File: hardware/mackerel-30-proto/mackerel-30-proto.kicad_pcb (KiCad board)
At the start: 2 copper layers, 160 x 100 mm, 73 parts, among them J1 Conn_01x02, J2 Conn_01x02, J3 Conn_02x05_Odd_Even, J4 Barrel_Jack_MountingPin, J5 Conn_02x05_Odd_Even, U1 MC68030RC, U10 MC68882, U2 EPM7128, U3 SST39SF040, U4 AS6C4008-55PCN, U5 XR68C681, U6 LM2576T-5, U7 AMS1117-3.3, U8 EPM7128, U9 SIMM72, X1 CXO_DIP14, X2 3.6864MHz, X3 CXO_DIP14

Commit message: positioning
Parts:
- added C27: C_Polarized, Capacitor_THT:CP_Radial_D5.0mm_P2.50mm, F.Cu at (-78.9, 88.3)
- added C28: C, Capacitor_THT:C_Disc_D4.3mm_W1.9mm_P5.00mm, F.Cu at (-57.9, 91.6)
- added D3: LED, LED_THT:LED_D5.0mm, F.Cu at (-64.5, 93.6)
- added HS1: Heatsink, Heatsink:Heatsink_Stonecold_HS-S02_13.21x9.53mm, F.Cu at (-67.0, 79.6)
- added J10: Conn_02x03_Odd_Even, Connector_PinHeader_2.54mm:PinHeader_2x03_P2.54mm_Vertical, F.Cu at (-64.3, 51.9)
- added J11: Conn_02x05_Odd_Even, Connector_IDC:IDC-Header_2x05_P2.54mm_Vertical, F.Cu at (-122.4, 15.6)
- added J6: Conn_02x10_Odd_Even, Connector_PinHeader_2.54mm:PinHeader_2x10_P2.54mm_Vertical, F.Cu at (-52.7, 103.2)
- added J7: Barrel_Jack_MountingPin, Connector_BarrelJack:BarrelJack_Horizontal, F.Cu at (-66.5, 64.6)
- added J8: Conn_02x03_Odd_Even, Connector_PinHeader_2.54mm:PinHeader_2x03_P2.54mm_Vertical, F.Cu at (-78.7, 51.9)
- added J9: Conn_02x03_Odd_Even, Connector_PinHeader_2.54mm:PinHeader_2x03_P2.54mm_Vertical, F.Cu at (-71.5, 51.9)
- added R23: R, Resistor_SMD:R_0805_2012Metric_Pad1.20x1.40mm_HandSolder, F.Cu at (-113.3, 28.2)
- added R24: R, Resistor_SMD:R_0805_2012Metric_Pad1.20x1.40mm_HandSolder, F.Cu at (-113.3, 31.1)
- added R25: R, Resistor_SMD:R_0805_2012Metric_Pad1.20x1.40mm_HandSolder, F.Cu at (-113.3, 34.1)
- added SW1: SW_Push, Button_Switch_THT:SW_PUSH_6mm_H5mm, F.Cu at (-90.8, 86.4)
- added U11: MC68882, Package_LCC:PLCC-68_THT-Socket, F.Cu at (84.4, 37.4)
- C1, C10, C11, C12, C13, C14, C15, C16, C17, C18, C19, C2, C20, C21, C22, C3, C4, C5, C6, C7, C8, C9: footprint Capacitor_SMD:C_1210_3225Metric_Pad1.33x2.70mm_HandSolder -> Capacitor_SMD:C_1206_3216Metric_Pad1.33x1.80mm_HandSolder
- J4: value Barrel_Jack_MountingPin -> Conn_01x06; footprint Connector_BarrelJack:BarrelJack_Horizontal -> Connector_PinHeader_2.54mm:PinHeader_1x06_P2.54mm_Vertical
- J5: value Conn_02x05_Odd_Even -> Conn_01x06; footprint Connector_IDC:IDC-Header_2x05_P2.54mm_Vertical -> Connector_PinHeader_2.54mm:PinHeader_1x06_P2.54mm_Vertical
- R1, R10, R11, R12, R13, R14, R15, R16, R17, R18, R19, R2, R20, R21, R22, R3, R4, R5, R6, R7, R8, R9: footprint Resistor_THT:R_Axial_DIN0207_L6.3mm_D2.5mm_P7.62mm_Horizontal -> Resistor_SMD:R_0805_2012Metric_Pad1.20x1.40mm_HandSolder
- U10: value MC68882 -> SIMM72; footprint Package_LCC:PLCC-68_THT-Socket -> mackerel:SIMM-72
- U8: value EPM7128 -> NE555P; footprint Package_LCC:PLCC-84_THT-Socket -> Package_DIP:DIP-8_W7.62mm
- U9: value SIMM72 -> EPM7128; footprint mackerel:SIMM-72 -> Package_LCC:PLCC-84_THT-Socket
- moved R22 384.8 mm to (-113.3, 25.2)
- moved J3 380.8 mm to (-109.6, 108.0)
- moved R14 372.9 mm to (-117.2, 112.2)
- moved R13 372.8 mm to (-117.2, 109.2)
- moved R12 372.8 mm to (-117.2, 106.3)
- moved R11 372.8 mm to (-117.2, 103.3)
- moved R19 368.9 mm to (-98.4, 85.8)
- moved R20 368.8 mm to (-98.4, 88.7)
- moved R21 368.8 mm to (-98.4, 91.7)
- moved J5 279.7 mm to (-15.3, 103.2)
- moved X2 276.0 mm to (-44.5, 137.4)
- moved U5 220.6 mm to (-33.8, 107.3)
- moved J4 176.4 mm to (-19.9, 103.2)
- moved U3 168.2 mm to (-98.7, 103.0), turned to 0 degrees
- moved U6 164.1 mm to (-90.5, 96.9)
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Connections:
- J4 pad 1: +12V -> GND
- J4 pad 2: GND -> /RTSA
- J4 pad 3: (no net) -> unconnected-(J4-Pin_3-Pad3)
- J5 pad 1: TCK_DRAM -> GND
- J5 pad 2: GND -> /RTSB
- J5 pad 3: TDO_DRAM -> unconnected-(J5-Pin_3-Pad3)
- J5 pad 4: +5V -> RXB
- J5 pad 5: TMS_DRAM -> TXB
- R19 pad 2: TDO_DRAM -> Net-(U8-R)
- R20 pad 1: +5V -> Net-(U8-THR)
- R20 pad 2: TMS_DRAM -> GND
- R21 pad 2: TDI_DRAM -> Net-(D3-A)
- R22 pad 1: TCK_DRAM -> +5V
- R22 pad 2: GND -> TDO_DRAM
- U10 pad 1: D2 -> GND
- U10 pad 12: GND -> DRAM_A0
- U10 pad 13: /RESET -> DRAM_A1
- U10 pad 14: GND -> DRAM_A2
- U10 pad 15: unconnected-(U10-NC-Pad15) -> DRAM_A3
- U10 pad 16: +5V -> DRAM_A4
- U10 pad 17: +5V -> DRAM_A5
- U10 pad 18: +5V -> DRAM_A6
- U10 pad 19: GND -> DRAM_A10
- U10 pad 2: D1 -> D0
- U10 pad 20: /DS -> D4
- U10 pad 21: /AS -> D20
- U10 pad 22: A4 -> D5
- U10 pad 23: A3 -> D21
- U10 pad 24: A2 -> D6
- U10 pad 25: A1 -> D22
- U10 pad 26: +5V -> D7
- U10 pad 27: +5V -> D23
- U10 pad 28: R/W -> DRAM_A7
- U10 pad 29: /CS_FPU -> DRAM_A11
- U10 pad 3: D0 -> D16
- U10 pad 30: GND -> +5V
- U10 pad 31: /DSACK0_FPU -> DRAM_A8
- U10 pad 32: /DSACK1_FPU -> DRAM_A9
- U10 pad 33: D31 -> /RAS3
- U10 pad 34: D30 -> /RAS1
- U10 pad 35: D29 -> unconnected-(U10-NC-Pad35)
- U10 pad 36: D28 -> unconnected-(U10-NC-Pad36)
- U10 pad 37: D27 -> unconnected-(U10-NC-Pad37)
- U10 pad 38: D26 -> unconnected-(U10-NC-Pad38)
- U10 pad 39: D25 -> GND
- U10 pad 4: GND -> D1
- U10 pad 40: D24 -> /CAS0
- U10 pad 41: GND -> /CAS2
- U10 pad 42: D23 -> /CAS3
- U10 pad 43: +5V -> /CAS1
- U10 pad 44: D22 -> /RAS0
- U10 pad 45: D21 -> /RAS2
- U10 pad 46: D20 -> unconnected-(U10-NC-Pad46)
- U10 pad 47: D19 -> DRAM_WR
- U10 pad 48: D18 -> unconnected-(U10-NC-Pad48)
- U10 pad 49: D17 -> D8
- U10 pad 5: GND -> D17
- U10 pad 50: D16 -> D24
- U10 pad 51: GND -> D9
- U10 pad 52: +5V -> D25
- U10 pad 53: +5V -> D10
- U10 pad 54: D15 -> D26
- U10 pad 55: D14 -> D11
- U10 pad 56: D13 -> D27
- U10 pad 58: D11 -> D28
- U10 pad 59: D10 -> +5V
- U10 pad 6: GND -> D2
- U10 pad 60: D9 -> D29
- U10 pad 61: +5V -> D13
- U10 pad 62: D8 -> D30
- U10 pad 63: GND -> D14
- U10 pad 64: D7 -> D31
- U10 pad 65: D6 -> D15
- U10 pad 66: D5 -> unconnected-(U10-NC-Pad66)
- U10 pad 67: D4 -> unconnected-(U10-PD1-Pad67)
- U10 pad 68: D3 -> unconnected-(U10-PD2-Pad68)
- U10 pad 7: GND -> D18
- U10 pad 8: GND -> D3
- U10 pad 9: GND -> D19
- U2 pad 10: /CS_DRAM -> unconnected-(U2-IO-Pad10)
- U2 pad 11: /DTACK_DRAM -> unconnected-(U2-IO-Pad11)
- U2 pad 12: /CS_DUART -> unconnected-(U2-IO-Pad12)
- U2 pad 15: /DTACK_DUART -> unconnected-(U2-IO-Pad15)
- U2 pad 16: /IRQ_DUART -> unconnected-(U2-IO-Pad16)
- U2 pad 17: /IACK_DUART -> unconnected-(U2-IO-Pad17)
- U2 pad 18: IDE_INT -> unconnected-(U2-IO-Pad18)
- U2 pad 20: /IDE_CS0 -> unconnected-(U2-IO-Pad20)
- U2 pad 21: IDE_RDY -> unconnected-(U2-IO-Pad21)
- U2 pad 22: /IDE_RD -> unconnected-(U2-IO-Pad22)
- U2 pad 24: /IDE_WR -> unconnected-(U2-IO-Pad24)
- U2 pad 25: /IDE_BUF -> unconnected-(U2-IO-Pad25)
- U2 pad 27: /CS_FPU -> unconnected-(U2-IO-Pad27)
- U2 pad 28: /DSACK0_FPU -> unconnected-(U2-IO-Pad28)
- U2 pad 29: /DSACK1_FPU -> unconnected-(U2-IO-Pad29)
- U2 pad 4: /CIIN -> unconnected-(U2-IO-Pad4)
- U2 pad 44: A0 -> unconnected-(U2-IO-Pad44)
- U2 pad 45: A1 -> unconnected-(U2-IO-Pad45)
- U2 pad 46: A2 -> unconnected-(U2-IO-Pad46)
- U2 pad 48: A3 -> unconnected-(U2-IO-Pad48)
- U2 pad 49: A16 -> unconnected-(U2-IO-Pad49)
- U2 pad 5: /STERM -> unconnected-(U2-IO-Pad5)
- U2 pad 50: A17 -> unconnected-(U2-IO-Pad50)
- U2 pad 51: A18 -> unconnected-(U2-IO-Pad51)
- U2 pad 52: A19 -> unconnected-(U2-IO-Pad52)
- U2 pad 54: A20 -> unconnected-(U2-IO-Pad54)
- U2 pad 55: A21 -> unconnected-(U2-IO-Pad55)
- U2 pad 56: A22 -> unconnected-(U2-IO-Pad56)
- U2 pad 57: A23 -> unconnected-(U2-IO-Pad57)
- U2 pad 58: A24 -> unconnected-(U2-IO-Pad58)
- U2 pad 60: A25 -> unconnected-(U2-IO-Pad60)
- U2 pad 61: A26 -> unconnected-(U2-IO-Pad61)
- U2 pad 63: A27 -> unconnected-(U2-IO-Pad63)
- U2 pad 64: /AS -> unconnected-(U2-IO-Pad64)
- U2 pad 65: /DS -> unconnected-(U2-IO-Pad65)
- U2 pad 67: R/W -> unconnected-(U2-IO-Pad67)
- U2 pad 68: /DSACK0 -> unconnected-(U2-IO-Pad68)
- U2 pad 69: /DSACK1 -> unconnected-(U2-IO-Pad69)
- U2 pad 70: SIZ0 -> unconnected-(U2-IO-Pad70)
- U2 pad 73: SIZ1 -> unconnected-(U2-IO-Pad73)
- U2 pad 74: /IPL0 -> unconnected-(U2-IO-Pad74)
- U2 pad 75: /IPL1 -> unconnected-(U2-IO-Pad75)
- U2 pad 76: /IPL2 -> unconnected-(U2-IO-Pad76)
- U2 pad 77: FC0 -> unconnected-(U2-IO-Pad77)
- U2 pad 79: FC1 -> unconnected-(U2-IO-Pad79)
- U2 pad 8: /CS_ROM -> unconnected-(U2-IO-Pad8)
- U2 pad 80: FC2 -> unconnected-(U2-IO-Pad80)
- U2 pad 81: /AVEC -> unconnected-(U2-IO-Pad81)
- U2 pad 9: /CS_SRAM -> unconnected-(U2-IO-Pad9)
- U5 pad 14: unconnected-(U5-OP1-Pad14) -> /RTSB
- U5 pad 15: unconnected-(U5-OP3-Pad15) -> OP3
- U5 pad 16: unconnected-(U5-OP5-Pad16) -> OP5
- U5 pad 17: unconnected-(U5-OP7-Pad17) -> OP7
- U5 pad 29: unconnected-(U5-OP6-Pad29) -> OP6
- U5 pad 3: unconnected-(U5-IP3-Pad3) -> IP3
- U5 pad 30: unconnected-(U5-OP4-Pad30) -> OP4
- U5 pad 31: unconnected-(U5-OP2-Pad31) -> OP2
- U5 pad 32: unconnected-(U5-OP0-Pad32) -> /RTSA
- U5 pad 40: unconnected-(U5-IP2-Pad40) -> IP2
- U5 pad 42: unconnected-(U5-IP5-Pad42) -> IP5
- U5 pad 43: unconnected-(U5-IP4-Pad43) -> IP4
- U5 pad 5: unconnected-(U5-IP1-Pad5) -> IP1
- U5 pad 8: unconnected-(U5-IP0-Pad8) -> IP0
- U8 pad 1: unconnected-(U8-GCLRn-Pad1) -> GND
- U8 pad 2: CLK_CPU -> Net-(U8-THR)
- U8 pad 3: +5V -> /RESET
- U8 pad 4: /RESET -> Net-(U8-R)
- U8 pad 5: /CS_DRAM -> unconnected-(U8-CV-Pad5)
- U8 pad 6: /DTACK_DRAM -> Net-(U8-THR)
- U8 pad 7: GND -> unconnected-(U8-DIS-Pad7)
- U8 pad 8: /AS -> +5V
- U9 pad 1: GND -> unconnected-(U9-GCLRn-Pad1)
- U9 pad 10: +5V -> R/W
- U9 pad 11: unconnected-(U9-NC-Pad11) -> SIZ0
- U9 pad 12: DRAM_A0 -> SIZ1
- U9 pad 13: DRAM_A1 -> +5V
- U9 pad 14: DRAM_A2 -> TDI_DRAM
- U9 pad 15: DRAM_A3 -> unconnected-(U9-IO-Pad15)
- U9 pad 16: DRAM_A4 -> unconnected-(U9-IO-Pad16)
- U9 pad 17: DRAM_A5 -> DRAM_A0
- U9 pad 18: DRAM_A6 -> DRAM_A1
- U9 pad 19: DRAM_A10 -> GND
- U9 pad 2: D0 -> CLK_CPU
- U9 pad 20: D4 -> DRAM_A2
- U9 pad 21: D20 -> DRAM_A3
- U9 pad 22: D5 -> DRAM_A4
- U9 pad 23: D21 -> TMS_DRAM
- U9 pad 24: D6 -> DRAM_A5
- U9 pad 25: D22 -> DRAM_A6
- U9 pad 26: D7 -> +5V
- U9 pad 27: D23 -> DRAM_A7
- U9 pad 28: DRAM_A7 -> DRAM_A8
- U9 pad 29: DRAM_A11 -> DRAM_A9
- U9 pad 3: D16 -> +5V
- U9 pad 30: +5V -> DRAM_A10
- U9 pad 31: DRAM_A8 -> DRAM_A11
- U9 pad 32: DRAM_A9 -> GND
- U9 pad 33: /RAS3 -> A0
- U9 pad 34: /RAS1 -> A1
- U9 pad 35: unconnected-(U9-NC-Pad35) -> A2
- U9 pad 36: unconnected-(U9-NC-Pad36) -> A3
- U9 pad 37: unconnected-(U9-NC-Pad37) -> A4
- U9 pad 38: unconnected-(U9-NC-Pad38) -> +5V
- U9 pad 39: GND -> A5
- U9 pad 4: D1 -> /RESET
- U9 pad 40: /CAS0 -> A6
- U9 pad 41: /CAS2 -> A7
- U9 pad 42: /CAS3 -> GND
- U9 pad 43: /CAS1 -> +5V
- U9 pad 44: /RAS0 -> A8
- U9 pad 45: /RAS2 -> A9
- U9 pad 46: unconnected-(U9-NC-Pad46) -> A10
- U9 pad 47: DRAM_WR -> GND
- U9 pad 48: unconnected-(U9-NC-Pad48) -> A11
- U9 pad 49: D8 -> A12
- U9 pad 5: D17 -> /CS_DRAM
- U9 pad 50: D24 -> A13
- U9 pad 51: D9 -> A14
- U9 pad 52: D25 -> A15
- U9 pad 53: D10 -> +5V
- U9 pad 54: D26 -> A16
- U9 pad 55: D11 -> A17
- U9 pad 56: D27 -> A18
- U9 pad 57: D12 -> A19
- U9 pad 58: D28 -> A20
- U9 pad 59: +5V -> GND
- U9 pad 6: D2 -> /DTACK_DRAM
- U9 pad 60: D29 -> A21
- U9 pad 61: D13 -> A22
- U9 pad 62: D30 -> TCK_DRAM
- U9 pad 63: D14 -> A23
- U9 pad 64: D31 -> A24
- U9 pad 65: D15 -> A25
- U9 pad 66: unconnected-(U9-NC-Pad66) -> +5V
- U9 pad 67: unconnected-(U9-PD1-Pad67) -> A26
- U9 pad 68: unconnected-(U9-PD2-Pad68) -> A27
- U9 pad 7: D18 -> GND
- U9 pad 70: unconnected-(U9-PD4-Pad70) -> /RAS0
- U9 pad 71: unconnected-(U9-NC-Pad71) -> TDO_DRAM
- U9 pad 8: D3 -> /AS
- U9 pad 9: D19 -> /DS
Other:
- board size 160 x 100 mm -> 2.4 x 113.8 mm

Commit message: Mostly fixed the SIMM-72 footprint
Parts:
- added C29: C, Capacitor_THT:C_Disc_D4.3mm_W1.9mm_P5.00mm, F.Cu at (-193.0, 80.2)
- added C30: C, Capacitor_THT:C_Disc_D4.3mm_W1.9mm_P5.00mm, F.Cu at (-193.0, 83.6)
- added C31: 1000uF, Capacitor_THT:CP_Radial_D10.0mm_P5.00mm, F.Cu at (-309.9, 58.5)
- added C32: 470uF, Capacitor_THT:CP_Radial_D8.0mm_P3.50mm, F.Cu at (-297.3, 59.3)
- added C33: 0.1uF, Capacitor_SMD:C_1206_3216Metric_Pad1.33x1.80mm_HandSolder, B.Cu at (264.8, 103.2)
- added C34: 0.1uF, Capacitor_SMD:C_1206_3216Metric_Pad1.33x1.80mm_HandSolder, B.Cu at (270.4, 116.2)
- added C35: 0.1uF, Capacitor_SMD:C_1206_3216Metric_Pad1.33x1.80mm_HandSolder, B.Cu at (245.0, 116.2)
- added C36: 0.1uF, Capacitor_SMD:C_1206_3216Metric_Pad1.33x1.80mm_HandSolder, B.Cu at (241.2, 102.2)
- added C37: 0.1uF, Capacitor_SMD:C_1206_3216Metric_Pad1.33x1.80mm_HandSolder, B.Cu at (241.2, 99.1)
- added C38: 0.1uF, Capacitor_SMD:C_1206_3216Metric_Pad1.33x1.80mm_HandSolder, B.Cu at (250.1, 100.7)
- added C39: 0.1uF, Capacitor_SMD:C_1206_3216Metric_Pad1.33x1.80mm_HandSolder, B.Cu at (266.6, 86.4)
- added D4: LED, LED_THT:LED_D5.0mm, F.Cu at (-192.1, 74.7)
- added J12: Screw_Terminal_01x04, TerminalBlock:TerminalBlock_bornier-4_P5.08mm, F.Cu at (-308.1, 72.1)
- added J13: Conn_02x20_Odd_Even, Connector_IDC:IDC-Header_2x20_P2.54mm_Vertical, F.Cu at (-279.3, 70.6)
- added R26: 4k7, Resistor_THT:R_Axial_DIN0207_L6.3mm_D2.5mm_P7.62mm_Horizontal, F.Cu at (-204.8, 74.9)
- added R27: 4k7, Resistor_THT:R_Axial_DIN0207_L6.3mm_D2.5mm_P7.62mm_Horizontal, F.Cu at (-204.8, 79.0)
- added R28: 470, Resistor_THT:R_Axial_DIN0207_L6.3mm_D2.5mm_P7.62mm_Horizontal, F.Cu at (-204.8, 83.0)
- added U12: 74HC245, Package_DIP:DIP-20_W7.62mm_Socket, F.Cu at (-309.8, 86.7)
- added U13: 74HC245, Package_DIP:DIP-20_W7.62mm_Socket, F.Cu at (-298.1, 86.7)
- C1, C10, C11, C12, C13, C14, C15, C16, C17, C18, C2, C3, C4, C5, C6, C7, C8, C9: moved to B.Cu
- moved C4 442.6 mm to (315.9, 103.4), turned to 180 degrees
- moved C5 442.5 mm to (315.9, 106.0), turned to 180 degrees
- moved C6 440.4 mm to (313.7, 111.0), turned to 180 degrees
- moved C3 440.2 mm to (313.9, 95.8), turned to 180 degrees
- moved C2 435.3 mm to (308.6, 95.8)
- moved C7 433.7 mm to (307.3, 109.7), turned to 90 degrees
- moved C1 431.1 mm to (303.8, 98.3)
- moved C8 424.6 mm to (302.3, 107.2), turned to 90 degrees
- moved C10 412.5 mm to (290.8, 107.3), turned to -90 degrees
- moved C9 411.9 mm to (290.8, 99.3), turned to 90 degrees
- moved C14 394.7 mm to (275.3, 46.4), turned to -90 degrees
- moved C15 386.5 mm to (273.7, 62.6)
- moved C13 385.3 mm to (265.4, 37.4), turned to 180 degrees
- moved C12 373.3 mm to (252.9, 29.1), turned to 180 degrees
- moved C16 368.3 mm to (255.4, 65.6), turned to 180 degrees
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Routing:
- net A1: track 0.00 -> 10.2 mm
- net D10: track 0.00 -> 10.1 mm
- net R/W: track 0.00 -> 9.99 mm
- net D30: track 0.00 -> 9.99 mm
- net D5: track 0.00 -> 9.84 mm
- net D7: track 0.00 -> 9.84 mm
- net D17: track 0.00 -> 8.16 mm
- net D14: track 0.00 -> 7.80 mm
- net D1: track 0.00 -> 7.76 mm
- net D24: track 0.00 -> 7.66 mm
- net D3: track 0.00 -> 7.55 mm
- net A3: track 0.00 -> 7.30 mm
- net D12: track 0.00 -> 7.30 mm
- net /RESET: track 0.00 -> 7.15 mm
- net /AS: track 0.00 -> 7.10 mm
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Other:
- board size 2.4 x 113.8 mm -> 180 x 120 mm
- copper layers 2 -> 4

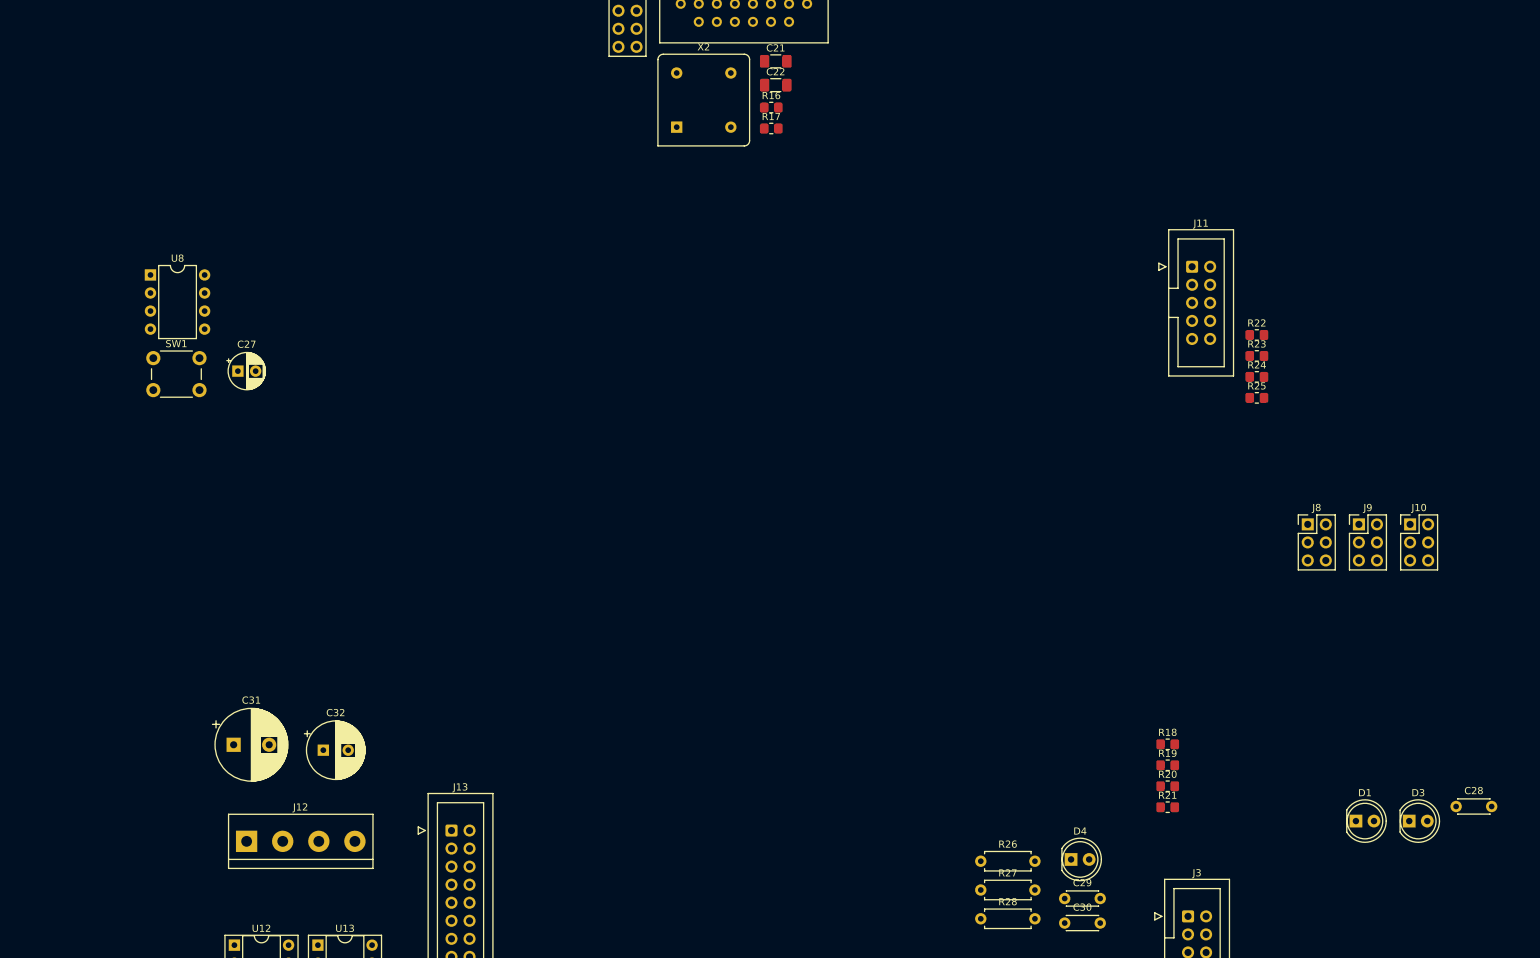
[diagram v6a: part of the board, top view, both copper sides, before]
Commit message: Add DS1233 for reset
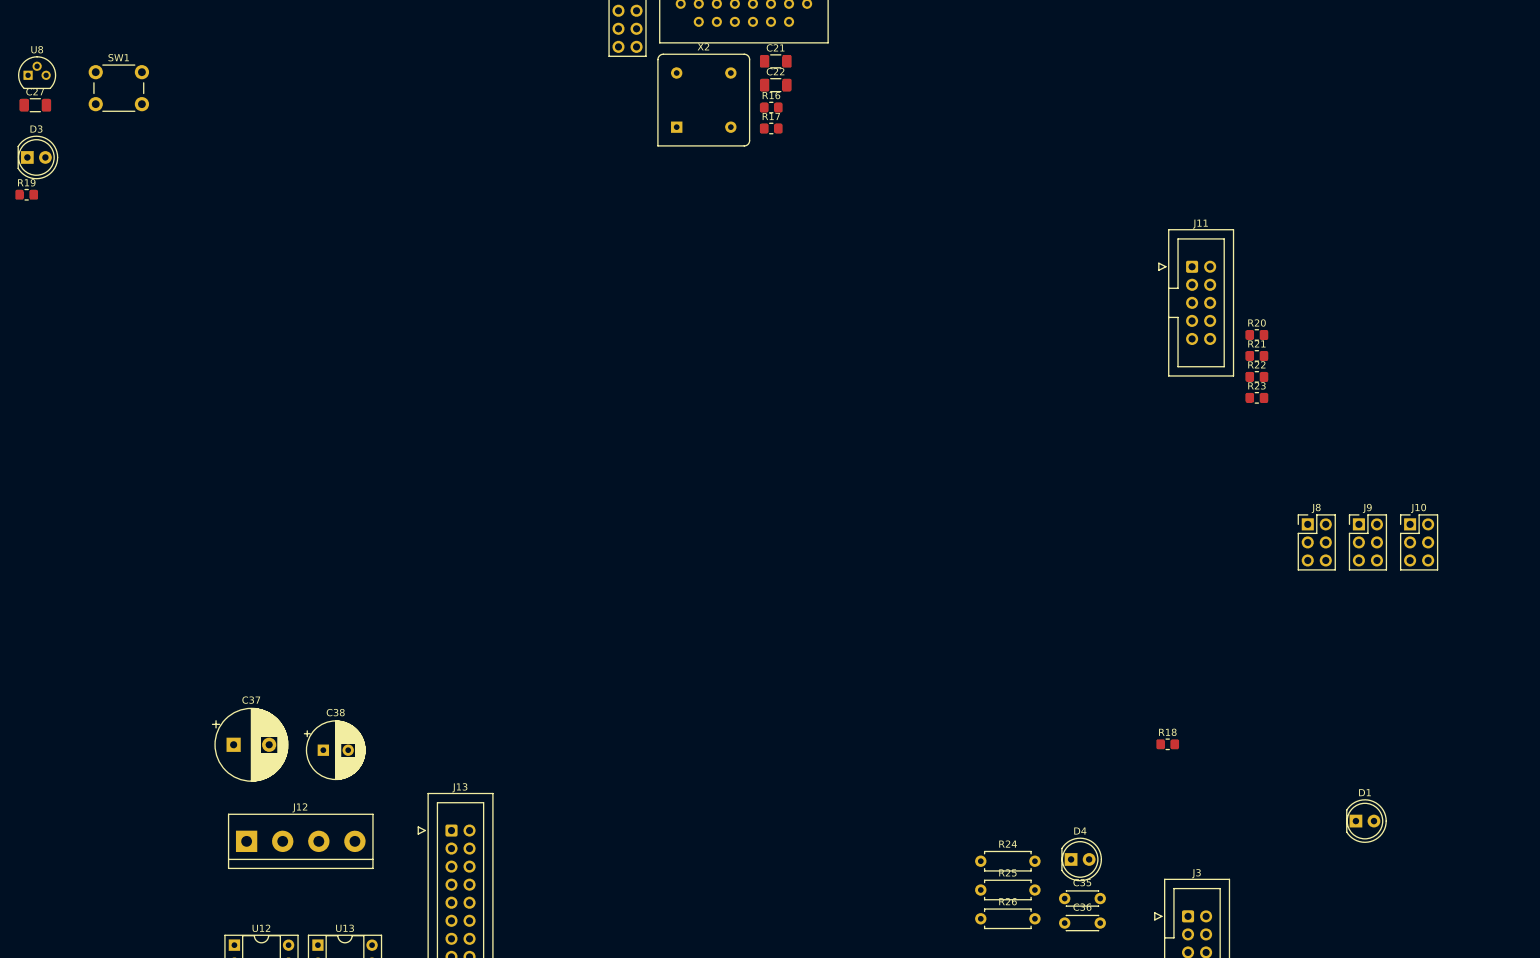
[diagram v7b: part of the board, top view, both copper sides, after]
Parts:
- removed the C28 at (-137.9, 67.2)
- removed the R20 at (-178.5, 64.4)
- removed the R21 at (-178.5, 67.3)
- C27: value C_Polarized -> 0.01uF; footprint Capacitor_THT:CP_Radial_D5.0mm_P2.50mm -> Capacitor_SMD:C_1206_3216Metric_Pad1.33x1.80mm_HandSolder
- R19: value R -> 1k
- U8: value NE555P -> DS1233; footprint Package_DIP:DIP-8_W7.62mm -> Package_TO_SOT_THT:TO-92
- moved D3 215.7 mm to (-339.0, -24.1)
- moved R19 179.5 mm to (-339.1, -18.8)
- moved C27 47.0 mm to (-337.8, -31.4)
- moved SW1 41.0 mm to (-329.3, -36.1)
- moved U8 33.0 mm to (-338.9, -35.7)
- renumbered C33 to C28, C34 to C29, C35 to C30, C36 to C31, C37 to C32, C38 to C33, C39 to C34, C29 to C35, C30 to C36, C31 to C37, C32 to C38, R22 to R20, R23 to R21, R24 to R22, R25 to R23, R26 to R24, R27 to R25, R28 to R26
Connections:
- C27 pad 1: +5V -> /RESET
- C27 pad 2: Net-(U8-THR) -> GND
- R19 pad 2: Net-(U8-R) -> Net-(D3-A)
- SW1 pad 1: GND -> /RESET
- SW1 pad 2: Net-(U8-R) -> GND
- U8 pad 2: Net-(U8-THR) -> /RESET
- U8 pad 3: /RESET -> +5V

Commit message: rough layout of the PCB components
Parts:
- removed R26: 470, Resistor_THT:R_Axial_DIN0207_L6.3mm_D2.5mm_P7.62mm_Horizontal
- added J14: DIN41612_03x32_ABC, Connector_DIN:DIN41612_C_3x32_Female_Vertical_THT, F.Cu at (38.2, 156.2)
- added U14: 74HC245, Package_DIP:DIP-20_W7.62mm_Socket, F.Cu at (38.3, 122.1)
- added U15: 74HC245, Package_DIP:DIP-20_W7.62mm_Socket, F.Cu at (50.1, 122.1)
- added U16: 74HC245, Package_DIP:DIP-20_W7.62mm_Socket, F.Cu at (61.8, 122.1)
- added U17: 74HC245, Package_DIP:DIP-20_W7.62mm_Socket, F.Cu at (73.6, 122.1)
- added U18: 74HC245, Package_DIP:DIP-20_W7.62mm_Socket, F.Cu at (85.3, 122.1)
- added U19: 74HC245, Package_DIP:DIP-20_W7.62mm_Socket, F.Cu at (97.1, 122.1)
- added U20: 74HC245, Package_DIP:DIP-20_W7.62mm_Socket, F.Cu at (108.8, 122.1)
- C1, C10, C11, C12, C13, C14, C15, C16, C17, C18, C2, C28, C29, C3, C30, C31, C32, C33, C34, C4, C5, C6, C7, C8, C9: footprint Capacitor_SMD:C_1206_3216Metric_Pad1.33x1.80mm_HandSolder -> Capacitor_THT:C_Disc_D4.3mm_W1.9mm_P5.00mm; moved to F.Cu
- C19, C20, C21, C22, C27: footprint Capacitor_SMD:C_1206_3216Metric_Pad1.33x1.80mm_HandSolder -> Capacitor_THT:C_Disc_D4.3mm_W1.9mm_P5.00mm
- R1, R11, R12, R13, R16, R18, R2, R20, R21, R22, R3, R4, R5, R6, R7, R8, R9: footprint Resistor_SMD:R_0805_2012Metric_Pad1.20x1.40mm_HandSolder -> Resistor_THT:R_Axial_DIN0207_L6.3mm_D2.5mm_P7.62mm_Horizontal
- R10, R15: value 4k7 -> R; footprint Resistor_SMD:R_0805_2012Metric_Pad1.20x1.40mm_HandSolder -> Resistor_THT:R_Axial_DIN0207_L6.3mm_D2.5mm_P7.62mm_Horizontal
- R14, R23: value R -> 4k7; footprint Resistor_SMD:R_0805_2012Metric_Pad1.20x1.40mm_HandSolder -> Resistor_THT:R_Axial_DIN0207_L6.3mm_D2.5mm_P7.62mm_Horizontal
- R17: value R -> 1k; footprint Resistor_SMD:R_0805_2012Metric_Pad1.20x1.40mm_HandSolder -> Resistor_THT:R_Axial_DIN0207_L6.3mm_D2.5mm_P7.62mm_Horizontal
- R19: value 1k -> R; footprint Resistor_SMD:R_0805_2012Metric_Pad1.20x1.40mm_HandSolder -> Resistor_THT:R_Axial_DIN0207_L6.3mm_D2.5mm_P7.62mm_Horizontal
- R25: value 4k7 -> 470
- moved C4 499.0 mm to (-181.0, 58.3), turned to 0 degrees
- moved C5 498.9 mm to (-181.0, 61.7), turned to 0 degrees
- moved C6 496.8 mm to (-181.0, 65.2), turned to 0 degrees
- moved C3 496.6 mm to (-181.0, 54.8), turned to 0 degrees
- moved C2 491.7 mm to (-181.0, 51.4)
- moved C1 487.5 mm to (-181.0, 47.9)
- moved C7 484.2 mm to (-172.9, 47.9), turned to 0 degrees
- moved C8 478.4 mm to (-172.9, 51.4), turned to 0 degrees
- moved C10 466.3 mm to (-172.9, 58.3), turned to 0 degrees
- moved C9 465.9 mm to (-172.9, 54.8), turned to 0 degrees
- moved C14 440.1 mm to (-164.7, 51.4), turned to 0 degrees
- moved C15 438.5 mm to (-164.7, 54.8)
- moved C13 430.3 mm to (-164.7, 47.9), turned to 0 degrees
- moved C12 427.3 mm to (-172.9, 65.2), turned to 0 degrees
- moved C16 420.2 mm to (-164.7, 58.3), turned to 0 degrees
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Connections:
- R10 pad 2: Net-(U1-/BGACK) -> TDO
- R11 pad 2: TDO -> TMS
- R12 pad 2: TMS -> TDI
- R13 pad 1: +5V -> TCK
- R13 pad 2: TDI -> GND
- R14 pad 1: TCK -> +5V
- R14 pad 2: GND -> Net-(U3-PGM)
- R15 pad 1: +5V -> /IACK_DUART
- R15 pad 2: Net-(U3-PGM) -> +5V
- R16 pad 1: /IACK_DUART -> /IRQ_DUART
- R17 pad 1: /IRQ_DUART -> +5V
- R17 pad 2: +5V -> Net-(D1-A)
- R18 pad 2: Net-(D1-A) -> Net-(D3-A)
- R19 pad 2: Net-(D3-A) -> TDO_DRAM
- R20 pad 2: TDO_DRAM -> TMS_DRAM
- R21 pad 2: TMS_DRAM -> TDI_DRAM
- R22 pad 1: +5V -> TCK_DRAM
- R22 pad 2: TDI_DRAM -> GND
- R23 pad 1: TCK_DRAM -> GND
- R23 pad 2: GND -> IDE_RDY
- R24 pad 2: IDE_RDY -> IDE_INT
- R25 pad 1: GND -> +5V
- R25 pad 2: IDE_INT -> Net-(D4-A)
- R4 pad 2: Net-(U1-/BERR) -> Net-(U1-/HALT)
- R5 pad 2: Net-(U1-/HALT) -> /IPL0
- R6 pad 2: /IPL0 -> /IPL1
- R7 pad 2: /IPL1 -> /IPL2
- R8 pad 2: /IPL2 -> Net-(U1-/BR)
- R9 pad 2: Net-(U1-/BR) -> Net-(U1-/BGACK)
- U1 pad A3: unconnected-(U1-A30-PadA3) -> A30
- U1 pad A4: unconnected-(U1-A28-PadA4) -> A28
- U1 pad B3: unconnected-(U1-A31-PadB3) -> A31
- U1 pad B4: unconnected-(U1-A29-PadB4) -> A29
- U1 pad H1: Net-(U1-/BERR) -> /BERR
- U2 pad 11: unconnected-(U2-IO-Pad11) -> /DTACK_DRAM
- U2 pad 12: unconnected-(U2-IO-Pad12) -> /CS_DUART
- U2 pad 15: unconnected-(U2-IO-Pad15) -> /DTACK_DUART
- U2 pad 16: unconnected-(U2-IO-Pad16) -> /IRQ_DUART
- U2 pad 17: unconnected-(U2-IO-Pad17) -> /IACK_DUART
- U2 pad 18: unconnected-(U2-IO-Pad18) -> IDE_INT
- U2 pad 20: unconnected-(U2-IO-Pad20) -> /IDE_CS0
- U2 pad 21: unconnected-(U2-IO-Pad21) -> /IDE_CS1
- U2 pad 22: unconnected-(U2-IO-Pad22) -> IDE_RDY
- U2 pad 24: unconnected-(U2-IO-Pad24) -> /IDE_RD
- U2 pad 25: unconnected-(U2-IO-Pad25) -> /IDE_WR
- U2 pad 27: unconnected-(U2-IO-Pad27) -> /IDE_BUF
- U2 pad 28: unconnected-(U2-IO-Pad28) -> /CS_FPU
- U2 pad 29: unconnected-(U2-IO-Pad29) -> /DSACK0_FPU
- U2 pad 30: unconnected-(U2-IO-Pad30) -> /DSACK1_FPU
- U2 pad 4: unconnected-(U2-IO-Pad4) -> /RESET
- U2 pad 49: unconnected-(U2-IO-Pad49) -> A0
- U2 pad 5: unconnected-(U2-IO-Pad5) -> /CIIN
- U2 pad 50: unconnected-(U2-IO-Pad50) -> A1
- U2 pad 51: unconnected-(U2-IO-Pad51) -> A2
- U2 pad 52: unconnected-(U2-IO-Pad52) -> A3
- U2 pad 54: unconnected-(U2-IO-Pad54) -> A16
- U2 pad 55: unconnected-(U2-IO-Pad55) -> A17
- U2 pad 56: unconnected-(U2-IO-Pad56) -> A18
- U2 pad 57: unconnected-(U2-IO-Pad57) -> A19
- U2 pad 58: unconnected-(U2-IO-Pad58) -> A28
- U2 pad 6: unconnected-(U2-IO-Pad6) -> /STERM
- U2 pad 60: unconnected-(U2-IO-Pad60) -> A29
- U2 pad 61: unconnected-(U2-IO-Pad61) -> A30
- U2 pad 63: unconnected-(U2-IO-Pad63) -> A31
- U2 pad 64: unconnected-(U2-IO-Pad64) -> /AS
- U2 pad 65: unconnected-(U2-IO-Pad65) -> /DS
- U2 pad 67: unconnected-(U2-IO-Pad67) -> R/W
- U2 pad 68: unconnected-(U2-IO-Pad68) -> /DSACK0
- U2 pad 69: unconnected-(U2-IO-Pad69) -> /DSACK1
- U2 pad 70: unconnected-(U2-IO-Pad70) -> SIZ0
- U2 pad 73: unconnected-(U2-IO-Pad73) -> SIZ1
- U2 pad 74: unconnected-(U2-IO-Pad74) -> /IPL0
- U2 pad 75: unconnected-(U2-IO-Pad75) -> /IPL1
- U2 pad 76: unconnected-(U2-IO-Pad76) -> /IPL2
- U2 pad 77: unconnected-(U2-IO-Pad77) -> FC0
- U2 pad 79: unconnected-(U2-IO-Pad79) -> FC1
- U2 pad 8: unconnected-(U2-IO-Pad8) -> /CS_ROM
- U2 pad 80: unconnected-(U2-IO-Pad80) -> FC2
- U2 pad 81: unconnected-(U2-IO-Pad81) -> /AVEC
- U2 pad 9: unconnected-(U2-IO-Pad9) -> /CS_SRAM
- U9 pad 10: R/W -> unconnected-(U9-IO-Pad10)
- U9 pad 11: SIZ0 -> unconnected-(U9-IO-Pad11)
- U9 pad 12: SIZ1 -> unconnected-(U9-IO-Pad12)
- U9 pad 17: DRAM_A0 -> unconnected-(U9-IO-Pad17)
- U9 pad 18: DRAM_A1 -> unconnected-(U9-IO-Pad18)
- U9 pad 20: DRAM_A2 -> unconnected-(U9-IO-Pad20)
- U9 pad 21: DRAM_A3 -> unconnected-(U9-IO-Pad21)
- U9 pad 22: DRAM_A4 -> unconnected-(U9-IO-Pad22)
- U9 pad 24: DRAM_A5 -> unconnected-(U9-IO-Pad24)
- U9 pad 25: DRAM_A6 -> unconnected-(U9-IO-Pad25)
- U9 pad 27: DRAM_A7 -> unconnected-(U9-IO-Pad27)
- U9 pad 28: DRAM_A8 -> unconnected-(U9-IO-Pad28)
- U9 pad 29: DRAM_A9 -> unconnected-(U9-IO-Pad29)
- U9 pad 30: DRAM_A10 -> unconnected-(U9-IO-Pad30)
- U9 pad 31: DRAM_A11 -> unconnected-(U9-IO-Pad31)
- U9 pad 35: A2 -> A26
- U9 pad 36: A3 -> A27
- U9 pad 37: A4 -> A24
- U9 pad 39: A5 -> A25
- U9 pad 4: /RESET -> unconnected-(U9-IO-Pad4)
- U9 pad 40: A6 -> A23
- U9 pad 41: A7 -> A22
- U9 pad 44: A8 -> A21
- U9 pad 45: A9 -> A20
- U9 pad 46: A10 -> A18
- U9 pad 48: A11 -> A19
- U9 pad 49: A12 -> A16
- U9 pad 5: /CS_DRAM -> unconnected-(U9-IO-Pad5)
- U9 pad 50: A13 -> A17
- U9 pad 52: A15 -> A11
- U9 pad 54: A16 -> A12
- U9 pad 55: A17 -> A15
- U9 pad 56: A18 -> A8
- U9 pad 57: A19 -> A13
- U9 pad 58: A20 -> A10
- U9 pad 6: /DTACK_DRAM -> unconnected-(U9-IO-Pad6)
- U9 pad 60: A21 -> A9
- U9 pad 61: A22 -> A7
- U9 pad 63: A23 -> A5
- U9 pad 64: A24 -> A3
- U9 pad 65: A25 -> A4
- U9 pad 67: A26 -> A2
- U9 pad 68: A27 -> unconnected-(U9-IO-Pad68)
- U9 pad 69: unconnected-(U9-IO-Pad69) -> A6
- U9 pad 70: /RAS0 -> unconnected-(U9-IO-Pad70)
- U9 pad 73: /RAS1 -> unconnected-(U9-IO-Pad73)
- U9 pad 74: /RAS2 -> unconnected-(U9-IO-Pad74)
- U9 pad 75: /RAS3 -> unconnected-(U9-IO-Pad75)
- U9 pad 76: /CAS0 -> unconnected-(U9-IO-Pad76)
- U9 pad 77: /CAS1 -> unconnected-(U9-IO-Pad77)
- U9 pad 79: /CAS2 -> unconnected-(U9-IO-Pad79)
- U9 pad 8: /AS -> unconnected-(U9-IO-Pad8)
- U9 pad 80: /CAS3 -> unconnected-(U9-IO-Pad80)
- U9 pad 81: DRAM_WR -> unconnected-(U9-IO-Pad81)
- U9 pad 9: /DS -> unconnected-(U9-IO-Pad9)
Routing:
- net A1: track 10.2 -> 0.00 mm
- net D10: track 10.1 -> 0.00 mm
- net R/W: track 9.99 -> 0.00 mm
- net D30: track 9.99 -> 0.00 mm
- net D5: track 9.84 -> 0.00 mm
- net D7: track 9.84 -> 0.00 mm
- net D17: track 8.16 -> 0.00 mm
- net D14: track 7.80 -> 0.00 mm
- net D1: track 7.76 -> 0.00 mm
- net D24: track 7.66 -> 0.00 mm
- net D3: track 7.55 -> 0.00 mm
- net A3: track 7.30 -> 0.00 mm
- net D12: track 7.30 -> 0.00 mm
- net /RESET: track 7.15 -> 0.00 mm
- net /AS: track 7.10 -> 0.00 mm
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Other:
- board size 180 x 120 mm -> 200 x 140 mm
